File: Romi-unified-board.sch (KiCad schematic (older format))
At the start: 74 parts, among them J1 ServoAnalog, J10 LIDAR_DATA, J11 LIDAR_MOTOR, J12 ROMI-Encoder, J13 ROMI-Encoder, J14 THING, J15 THING, J16 Conn_01x03_Male, J17 Conn_01x03_Male, J18 Conn_01x03_Male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

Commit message: added fiducials
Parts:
- added FID1, FID2: Fiducial, Fiducial:Fiducial_1mm_Mask2mm, symbol Mechanical:Fiducial
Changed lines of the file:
@@
 	0    -1   -1   0
 $EndComp
+$Comp
+L Mechanical:Fiducial FID1
+U 1 1 5F9E5F74
+P 4200 1050
+F 0 "FID1" H 4285 1096 50  0000 L CNN
+F 1 "Fiducial" H 4285 1005 50  0000 L CNN
+F 2 "Fiducial:Fiducial_1mm_Mask2mm" H 4200 1050 50  0001 C CNN
+F 3 "~" H 4200 1050 50  0001 C CNN
+	1    4200 1050
+	1    0    0    -1
+$EndComp
+$Comp
+L Mechanical:Fiducial FID2
+U 1 1 5F9E62BB
+P 5000 1100
+F 0 "FID2" H 5085 1146 50  0000 L CNN
+F 1 "Fiducial" H 5085 1055 50  0000 L CNN
+F 2 "Fiducial:Fiducial_1mm_Mask2mm" H 5000 1100 50  0001 C CNN
+F 3 "~" H 5000 1100 50  0001 C CNN
+	1    5000 1100
+	1    0    0    -1
+$EndComp
 $EndSCHEMATC

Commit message: Fixed error in netlist.
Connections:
- wire segments 269 -> 272
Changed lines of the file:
@@
 	1    0    0    -1
 $EndComp
+Wire Wire Line
+	1750 3050 1700 3050
+Wire Wire Line
+	1750 3150 1700 3150
+Wire Wire Line
+	1750 3250 1700 3250
 $EndSCHEMATC

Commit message: Swapped pins 16 and 17
#10
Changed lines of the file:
@@
 Text GLabel 13200 3050 2    50   Input ~ 0
 GPIO26
+Text GLabel 6100 -300 2    50   Input ~ 0
+GPIO17
 Text GLabel 5700 -150 2    50   Input ~ 0
-GPIO17
-Text GLabel 6100 -300 2    50   Input ~ 0
 GPIO16
 Wire Wire Line

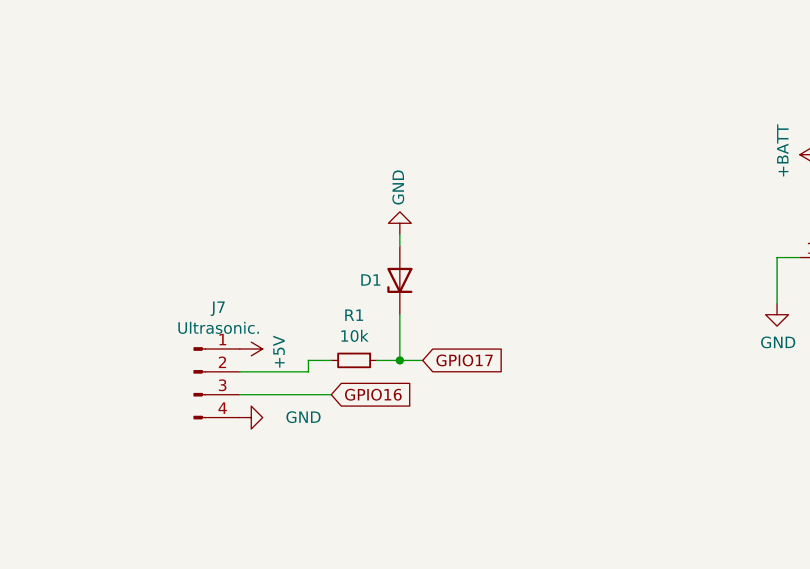
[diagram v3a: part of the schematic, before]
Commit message: Fixed  ultrasonic
#10
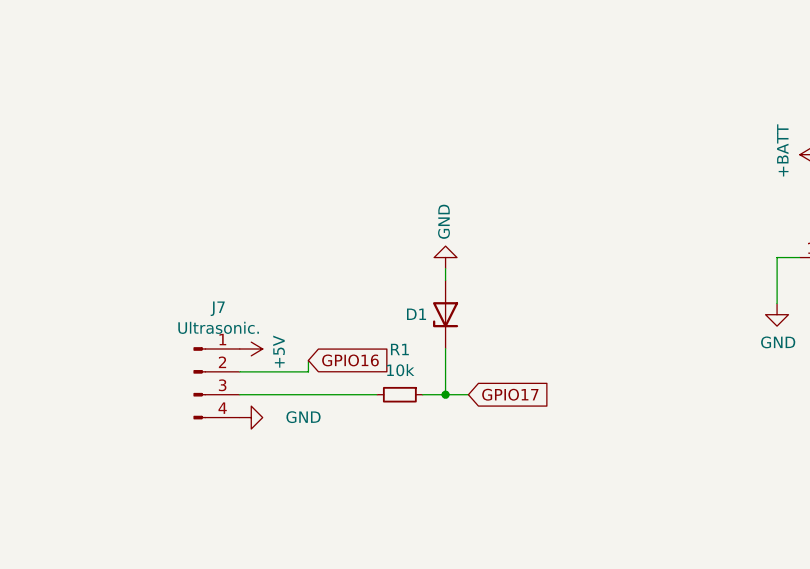
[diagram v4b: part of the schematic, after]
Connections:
- wire segments 272 -> 271
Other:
- moved on the sheet: D1, R1
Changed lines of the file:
@@
 Text GLabel 13200 3050 2    50   Input ~ 0
 GPIO26
-Text GLabel 6100 -300 2    50   Input ~ 0
+Text GLabel 6300 -150 2    50   Input ~ 0
 GPIO17
-Text GLabel 5700 -150 2    50   Input ~ 0
+Text GLabel 5600 -300 2    50   Input ~ 0
 GPIO16
 Wire Wire Line
@@
 L Device:R_Small R1
 U 1 1 5F1ADAC2
-P 5800 -300
-F 0 "R1" V 5604 -300 50  0000 C CNN
-F 1 "10k" V 5695 -300 50  0000 C CNN
-F 2 "Resistor_SMD:R_0603_1608Metric" H 5800 -300 50  0001 C CNN
-F 3 "~" H 5800 -300 50  0001 C CNN
-	1    5800 -300
+P 6000 -150
+F 0 "R1" V 5804 -150 50  0000 C CNN
+F 1 "10k" V 5895 -150 50  0000 C CNN
+F 2 "Resistor_SMD:R_0603_1608Metric" H 6000 -150 50  0001 C CNN
+F 3 "~" H 6000 -150 50  0001 C CNN
+	1    6000 -150
 	0    1    1    0
 $EndComp
@@
 L Device:D_Zener D1
 U 1 1 5F1ECB50
-P 6000 -650
-F 0 "D1" V 6000 -571 50  0000 L CNN
-F 1 "D_Zener" V 6045 -571 50  0001 L CNN
-F 2 "Diode_SMD:D_SOD-323F" H 6000 -650 50  0001 C CNN
-F 3 "~" H 6000 -650 50  0001 C CNN
-	1    6000 -650
+P 6200 -500
+F 0 "D1" V 6200 -421 50  0000 L CNN
+F 1 "D_Zener" V 6245 -421 50  0001 L CNN
+F 2 "Diode_SMD:D_SOD-323F" H 6200 -500 50  0001 C CNN
+F 3 "~" H 6200 -500 50  0001 C CNN
+	1    6200 -500
 	0    -1   -1   0
 $EndComp
@@
 L power:GND #PWR0132
 U 1 1 5F1EDCD3
-P 6000 -850
-F 0 "#PWR0132" H 6000 -1100 50  0001 C CNN
-F 1 "GND" V 6005 -978 50  0000 R CNN
-F 2 "" H 6000 -850 50  0001 C CNN
-F 3 "" H 6000 -850 50  0001 C CNN
-	1    6000 -850
+P 6200 -700
+F 0 "#PWR0132" H 6200 -950 50  0001 C CNN
+F 1 "GND" V 6205 -828 50  0000 R CNN
+F 2 "" H 6200 -700 50  0001 C CNN
+F 3 "" H 6200 -700 50  0001 C CNN
+	1    6200 -700
 	-1   0    0    1
 $EndComp
 Wire Wire Line
-	5900 -300 6000 -300
-Wire Wire Line
-	6000 -500 6000 -300
-Connection ~ 6000 -300
-Wire Wire Line
-	6000 -300 6100 -300
-Wire Wire Line
-	6000 -850 6000 -800
+	6100 -150 6200 -150
+Wire Wire Line
+	6200 -350 6200 -150
+Connection ~ 6200 -150
+Wire Wire Line
+	6200 -150 6300 -150
+Wire Wire Line
+	6200 -700 6200 -650
 Text GLabel 6350 1000 2    50   Input ~ 0
 GPIO23
@@
 Connection ~ 5250 5600
 Wire Wire Line
-	5700 -300 5600 -300
-Wire Wire Line
 	5600 -300 5600 -250
 Wire Wire Line
 	5600 -250 5300 -250
-Wire Wire Line
-	5700 -150 5300 -150
 Wire Wire Line
 	12650 5000 13000 5000
@@
 Wire Wire Line
 	1750 3250 1700 3250
+Wire Wire Line
+	5300 -150 5900 -150
 $EndSCHEMATC

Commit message: Batch of changes
Fixed Switch footprint
Swapped left and right H bridges to match shim.
Updated silkscreen
Fixed ultrasonic pinout.
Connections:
- net labels added: +5VL
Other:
- note added: "ELA\n"
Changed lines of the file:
@@
 GND
 Text Notes 12250 3100 0    50   ~ 0
-ELA
+ELB
 Text Notes 12250 3200 0    50   ~ 0
-ELB
+ELA\n
 Text Notes 12100 3300 0    50   ~ 0
 VCCENC
@@
 GND
 Text Notes 12250 4950 0    50   ~ 0
+ELB
+Text Notes 12250 5050 0    50   ~ 0
 ELA
-Text Notes 12250 5050 0    50   ~ 0
-ELB
 Text Notes 12100 5150 0    50   ~ 0
 VCCENC
@@
 Wire Wire Line
 	13150 4800 12650 4800
+Text GLabel 14700 3000 0    50   Input ~ 0
+GPIO12
+Text GLabel 14700 2900 0    50   Input ~ 0
+GPIO25
+Text GLabel 16750 2900 0    50   Input ~ 0
+GPIO4
 Text GLabel 16750 3000 0    50   Input ~ 0
-GPIO12
-Text GLabel 16750 2900 0    50   Input ~ 0
-GPIO25
-Text GLabel 14700 2900 0    50   Input ~ 0
-GPIO4
-Text GLabel 14700 3000 0    50   Input ~ 0
 GPIO13
 $Comp
@@
 Text GLabel 1700 3450 0    50   Input ~ 0
 GPIO13
-$Comp
-L power:+5V #PWR0126
-U 1 1 5F04D5C5
-P 1350 3850
-F 0 "#PWR0126" H 1350 3700 50  0001 C CNN
-F 1 "+5V" V 1365 3978 50  0000 L CNN
-F 2 "" H 1350 3850 50  0001 C CNN
-F 3 "" H 1350 3850 50  0001 C CNN
-	1    1350 3850
-	0    -1   -1   0
-$EndComp
 Wire Wire Line
 	1750 3850 1350 3850
@@
 GPIO21
 $Comp
-L power:+5V #PWR0131
-U 1 1 5F1AA820
-P 5300 -350
-F 0 "#PWR0131" H 5300 -500 50  0001 C CNN
-F 1 "+5V" H 5315 -177 50  0000 C CNN
-F 2 "" H 5300 -350 50  0001 C CNN
-F 3 "" H 5300 -350 50  0001 C CNN
-	1    5300 -350
-	0    1    1    0
-$EndComp
-$Comp
 L Device:R_Small R1
 U 1 1 5F1ADAC2
@@
 Wire Wire Line
 	2400 3150 2400 3450
-Text Notes 2500 4050 0    50   ~ 0
+Text Notes 2500 4300 0    50   ~ 0
 VUSB connects right to the plug.\nWe can't hook it up to 5v.\nWe drop the 5v by about a \nvolt and feed it into the BAT pin.
 NoConn ~ 2600 2950
@@
 Wire Wire Line
 	5300 -150 5900 -150
+$Comp
+L power:+5VL #PWR0126
+U 1 1 5F9F68D9
+P 5300 -350
+F 0 "#PWR0126" H 5300 -500 50  0001 C CNN
+F 1 "+5VL" V 5315 -222 50  0000 L CNN
+F 2 "" H 5300 -350 50  0001 C CNN
+F 3 "" H 5300 -350 50  0001 C CNN
+	1    5300 -350
+	0    1    1    0
+$EndComp
+$Comp
+L power:+5VL #PWR0131
+U 1 1 5F9F7789
+P 1350 3850
+F 0 "#PWR0131" H 1350 3700 50  0001 C CNN
+F 1 "+5VL" V 1365 3977 50  0000 L CNN
+F 2 "" H 1350 3850 50  0001 C CNN
+F 3 "" H 1350 3850 50  0001 C CNN
+	1    1350 3850
+	0    -1   -1   0
+$EndComp
+$Comp
+L power:+5VL #PWR0162
+U 1 1 5F9F99D1
+P 2400 3800
+F 0 "#PWR0162" H 2400 3650 50  0001 C CNN
+F 1 "+5VL" V 2415 3928 50  0000 L CNN
+F 2 "" H 2400 3800 50  0001 C CNN
+F 3 "" H 2400 3800 50  0001 C CNN
+	1    2400 3800
+	0    1    1    0
+$EndComp
+Connection ~ 2400 3800
 $EndSCHEMATC

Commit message: Minor Changes
Updated switch part.
Removed LIDAR connector and IMU.
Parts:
- removed C21: 0.1u, Capacitor_SMD:C_0603_1608Metric, symbol Device:C
- removed H1, H2: MountingHole, MountingHole:MountingHole_2.2mm_M2_DIN965, symbol Mechanical:MountingHole
- removed J10: LIDAR_DATA, unified:JST_BM06B-GHS-TBT(LF)(SN)(N), symbol Connector:Conn_01x06_Male
- removed J11: LIDAR_MOTOR, unified:JST_SM02B-PASS-TBT(LF)(SN), symbol Connector:Conn_01x02_Male
- removed U5: LSM6DS33TR, unified:PQFN50P300X300X86-16N, symbol LSM6DS33TR:LSM6DS33TR
- SW1, SW2, SW3: footprint unified:CSS-1210TB -> unified:SK3296S01L1
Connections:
- wire segments 271 -> 258
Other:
- note removed: "BM06B-GHS-TBT(LF)(SN)(N)"
- note removed: "SM02B-PASS-TBT(LF)(SN)\n"
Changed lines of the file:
@@
 F 0 "SW1" H 7950 -515 50  0000 C CNN
 F 1 "SW_SPST" H 7950 -606 50  0000 C CNN
-F 2 "unified:CSS-1210TB" H 7950 -750 50  0001 C CNN
+F 2 "unified:SK3296S01L1" H 7950 -750 50  0001 C CNN
 F 3 "~" H 7950 -750 50  0001 C CNN
 	1    7950 -750
@@
 Wire Wire Line
 	6300 1300 6350 1300
-$Comp
-L Mechanical:MountingHole H2
-U 1 1 5EF4C5E3
-P 5200 4200
-F 0 "H2" H 5300 4246 50  0000 L CNN
-F 1 "MountingHole" H 5300 4155 50  0000 L CNN
-F 2 "MountingHole:MountingHole_2.2mm_M2_DIN965" H 5200 4200 50  0001 C CNN
-F 3 "~" H 5200 4200 50  0001 C CNN
-	1    5200 4200
-	1    0    0    -1
-$EndComp
 Text Notes 8650 -1150 0    50   ~ 0
 trig
@@
 	6350 1400 6300 1400
 $Comp
-L Connector:Conn_01x06_Male J10
-U 1 1 5F7D63BD
-P 10150 1500
-F 0 "J10" H 10258 1881 50  0000 C CNN
-F 1 "LIDAR_DATA" H 10258 1790 50  0000 C CNN
-F 2 "unified:JST_BM06B-GHS-TBT(LF)(SN)(N)" H 10150 1500 50  0001 C CNN
-F 3 "~" H 10150 1500 50  0001 C CNN
-	1    10150 1500
-	1    0    0    -1
-$EndComp
-$Comp
-L Connector:Conn_01x02_Male J11
-U 1 1 5F7D9E2D
-P 10150 2150
-F 0 "J11" H 10258 2331 50  0000 C CNN
-F 1 "LIDAR_MOTOR" H 10258 2240 50  0000 C CNN
-F 2 "unified:JST_SM02B-PASS-TBT(LF)(SN)" H 10150 2150 50  0001 C CNN
-F 3 "~" H 10150 2150 50  0001 C CNN
-	1    10150 2150
-	1    0    0    -1
-$EndComp
-$Comp
-L power:+5V #PWR0138
-U 1 1 5F7DA3E0
-P 10500 1800
-F 0 "#PWR0138" H 10500 1650 50  0001 C CNN
-F 1 "+5V" H 10515 1973 50  0000 C CNN
-F 2 "" H 10500 1800 50  0001 C CNN
-F 3 "" H 10500 1800 50  0001 C CNN
-	1    10500 1800
-	0    1    1    0
-$EndComp
-$Comp
-L power:+5V #PWR0139
-U 1 1 5F7DB526
-P 10500 2250
-F 0 "#PWR0139" H 10500 2100 50  0001 C CNN
-F 1 "+5V" H 10515 2423 50  0000 C CNN
-F 2 "" H 10500 2250 50  0001 C CNN
-F 3 "" H 10500 2250 50  0001 C CNN
-	1    10500 2250
-	0    1    1    0
-$EndComp
-Wire Wire Line
-	10350 1600 11150 1600
-Wire Wire Line
-	11150 1600 11150 2150
-Wire Wire Line
-	11150 2150 10350 2150
-Wire Wire Line
-	10500 1800 10350 1800
-Wire Wire Line
-	10500 2250 10350 2250
-Text GLabel 10350 1700 2    50   Input ~ 0
-GPIO16
-Text GLabel 10350 1400 2    50   Input ~ 0
-GPIO17
-$Comp
-L power:GND #PWR0140
-U 1 1 5F80E676
-P 10600 1500
-F 0 "#PWR0140" H 10600 1250 50  0001 C CNN
-F 1 "GND" V 10605 1372 50  0000 R CNN
-F 2 "" H 10600 1500 50  0001 C CNN
-F 3 "" H 10600 1500 50  0001 C CNN
-	1    10600 1500
-	0    -1   -1   0
-$EndComp
-Wire Wire Line
-	10350 1500 10600 1500
-$Comp
 L Connector_Generic:Conn_02x19_Odd_Even J6
 U 1 1 5F64EE4F
@@
 	-1   0    0    -1
 $EndComp
-Text Notes 8950 1550 0    50   ~ 0
-BM06B-GHS-TBT(LF)(SN)(N)
-Text Notes 9000 2200 0    50   ~ 0
-SM02B-PASS-TBT(LF)(SN)\n
 $Comp
 L Transistor_FET:SiS415DNT Q2
@@
 SDA
 $Comp
-L power:GND #PWR0172
-U 1 1 5FAEFB38
-P 20250 -1350
-F 0 "#PWR0172" H 20250 -1600 50  0001 C CNN
-F 1 "GND" V 20255 -1478 50  0000 R CNN
-F 2 "" H 20250 -1350 50  0001 C CNN
-F 3 "" H 20250 -1350 50  0001 C CNN
-	1    20250 -1350
-	1    0    0    -1
-$EndComp
-$Comp
-L power:+3.3V #PWR0173
-U 1 1 5FAEFF10
-P 20250 -2150
-F 0 "#PWR0173" H 20250 -2300 50  0001 C CNN
-F 1 "+3.3V" V 20265 -2022 50  0000 L CNN
-F 2 "" H 20250 -2150 50  0001 C CNN
-F 3 "" H 20250 -2150 50  0001 C CNN
-	1    20250 -2150
-	0    1    1    0
-$EndComp
-Text GLabel 18950 -1750 0    50   Input ~ 0
-SDA
-Text GLabel 18950 -1850 0    50   Input ~ 0
-GPIO22
-$Comp
-L Device:C C21
-U 1 1 5FC7F43B
-P 18200 -2800
-F 0 "C21" H 18315 -2754 50  0000 L CNN
-F 1 "0.1u" H 18315 -2845 50  0000 L CNN
-F 2 "Capacitor_SMD:C_0603_1608Metric" H 18238 -2950 50  0001 C CNN
-F 3 "~" H 18200 -2800 50  0001 C CNN
-	1    18200 -2800
-	1    0    0    -1
-$EndComp
-$Comp
-L power:+3.3V #PWR0176
-U 1 1 5FC80AFF
-P 18200 -2950
-F 0 "#PWR0176" H 18200 -3100 50  0001 C CNN
-F 1 "+3.3V" V 18215 -2822 50  0000 L CNN
-F 2 "" H 18200 -2950 50  0001 C CNN
-F 3 "" H 18200 -2950 50  0001 C CNN
-	1    18200 -2950
-	1    0    0    -1
-$EndComp
-$Comp
-L power:GND #PWR0177
-U 1 1 5FC80F9A
-P 18200 -2650
-F 0 "#PWR0177" H 18200 -2900 50  0001 C CNN
-F 1 "GND" V 18205 -2778 50  0000 R CNN
-F 2 "" H 18200 -2650 50  0001 C CNN
-F 3 "" H 18200 -2650 50  0001 C CNN
-	1    18200 -2650
-	1    0    0    -1
-$EndComp
-$Comp
 L power:+3.3V #PWR0102
 U 1 1 5FE209CF
@@
 	6400 2650 6300 2650
 $Comp
-L Mechanical:MountingHole H1
-U 1 1 5EF4C315
-P 5550 4000
-F 0 "H1" H 5650 4046 50  0000 L CNN
-F 1 "MountingHole" H 5750 3900 50  0000 L CNN
-F 2 "MountingHole:MountingHole_2.2mm_M2_DIN965" H 5550 4000 50  0001 C CNN
-F 3 "~" H 5550 4000 50  0001 C CNN
-	1    5550 4000
-	1    0    0    -1
-$EndComp
-$Comp
 L Switch:SW_SPDT SW2
 U 1 1 5F890447
@@
 F 0 "SW2" H 3450 7435 50  0000 C CNN
 F 1 "SW_SPDT" H 3450 7344 50  0000 C CNN
-F 2 "unified:CSS-1210TB" H 3450 7150 50  0001 C CNN
+F 2 "unified:SK3296S01L1" H 3450 7150 50  0001 C CNN
 F 3 "~" H 3450 7150 50  0001 C CNN
 	1    3450 7150
@@
 F 0 "SW3" H 13550 1835 50  0000 C CNN
 F 1 "SW_SPST" H 13550 1744 50  0000 C CNN
-F 2 "unified:CSS-1210TB" H 13550 1600 50  0001 C CNN
+F 2 "unified:SK3296S01L1" H 13550 1600 50  0001 C CNN
 F 3 "~" H 13550 1600 50  0001 C CNN
 	1    13550 1600
@@
 	2750 -450 2600 -450
 $Comp
-L LSM6DS33TR:LSM6DS33TR U5
-U 1 1 5FA8D316
-P 19550 -1750
-F 0 "U5" H 19550 -1083 50  0000 C CNN
-F 1 "LSM6DS33TR" H 19550 -1174 50  0000 C CNN
-F 2 "unified:PQFN50P300X300X86-16N" H 19550 -1750 50  0001 L BNN
-F 3 "6" H 19550 -1750 50  0001 L BNN
-F 4 "STMicroelectronics" H 19550 -1750 50  0001 L BNN "Field4"
-F 5 "IPC-7351B" H 19550 -1750 50  0001 L BNN "Field5"
-	1    19550 -1750
-	1    0    0    -1
-$EndComp
-Wire Wire Line
-	20250 -2150 20200 -2150
-Wire Wire Line
-	20150 -2050 20200 -2050
-Wire Wire Line
-	20200 -2050 20200 -2150
-Connection ~ 20200 -2150
-Wire Wire Line
-	20200 -2150 20150 -2150
-Wire Wire Line
-	20150 -1550 20250 -1550
-Wire Wire Line
-	20250 -1550 20250 -1350
-Wire Wire Line
-	20150 -1350 20250 -1350
-Connection ~ 20250 -1350
-$Comp
-L power:+3.3V #PWR0174
-U 1 1 5FC03884
-P 18950 -1550
-F 0 "#PWR0174" H 18950 -1700 50  0001 C CNN
-F 1 "+3.3V" V 18965 -1422 50  0000 L CNN
-F 2 "" H 18950 -1550 50  0001 C CNN
-F 3 "" H 18950 -1550 50  0001 C CNN
-	1    18950 -1550
-	0    -1   -1   0
-$EndComp
-$Comp
 L Mechanical:Fiducial FID1
